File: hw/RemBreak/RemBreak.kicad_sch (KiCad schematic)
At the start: 5 parts, among them J1 Conn_02x06_Odd_Even, J2 Screw_Terminal_01x04, J3 Screw_Terminal_01x04

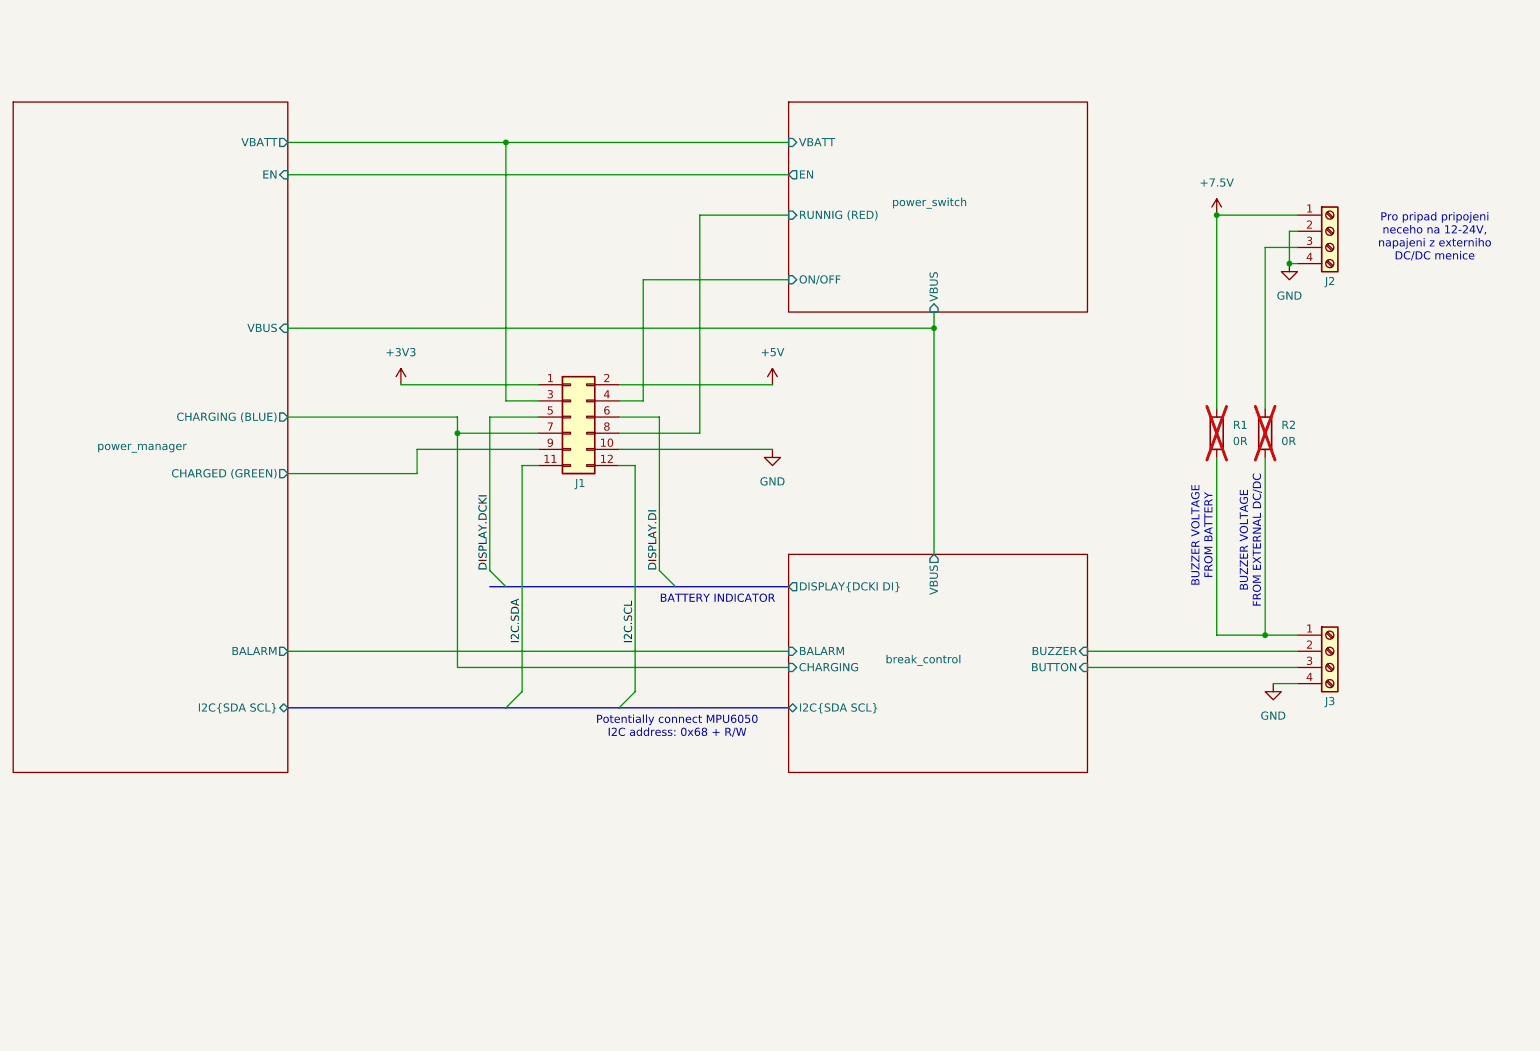
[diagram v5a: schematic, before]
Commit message: routing in progress added new subsheet to easily swap signals at the control connector
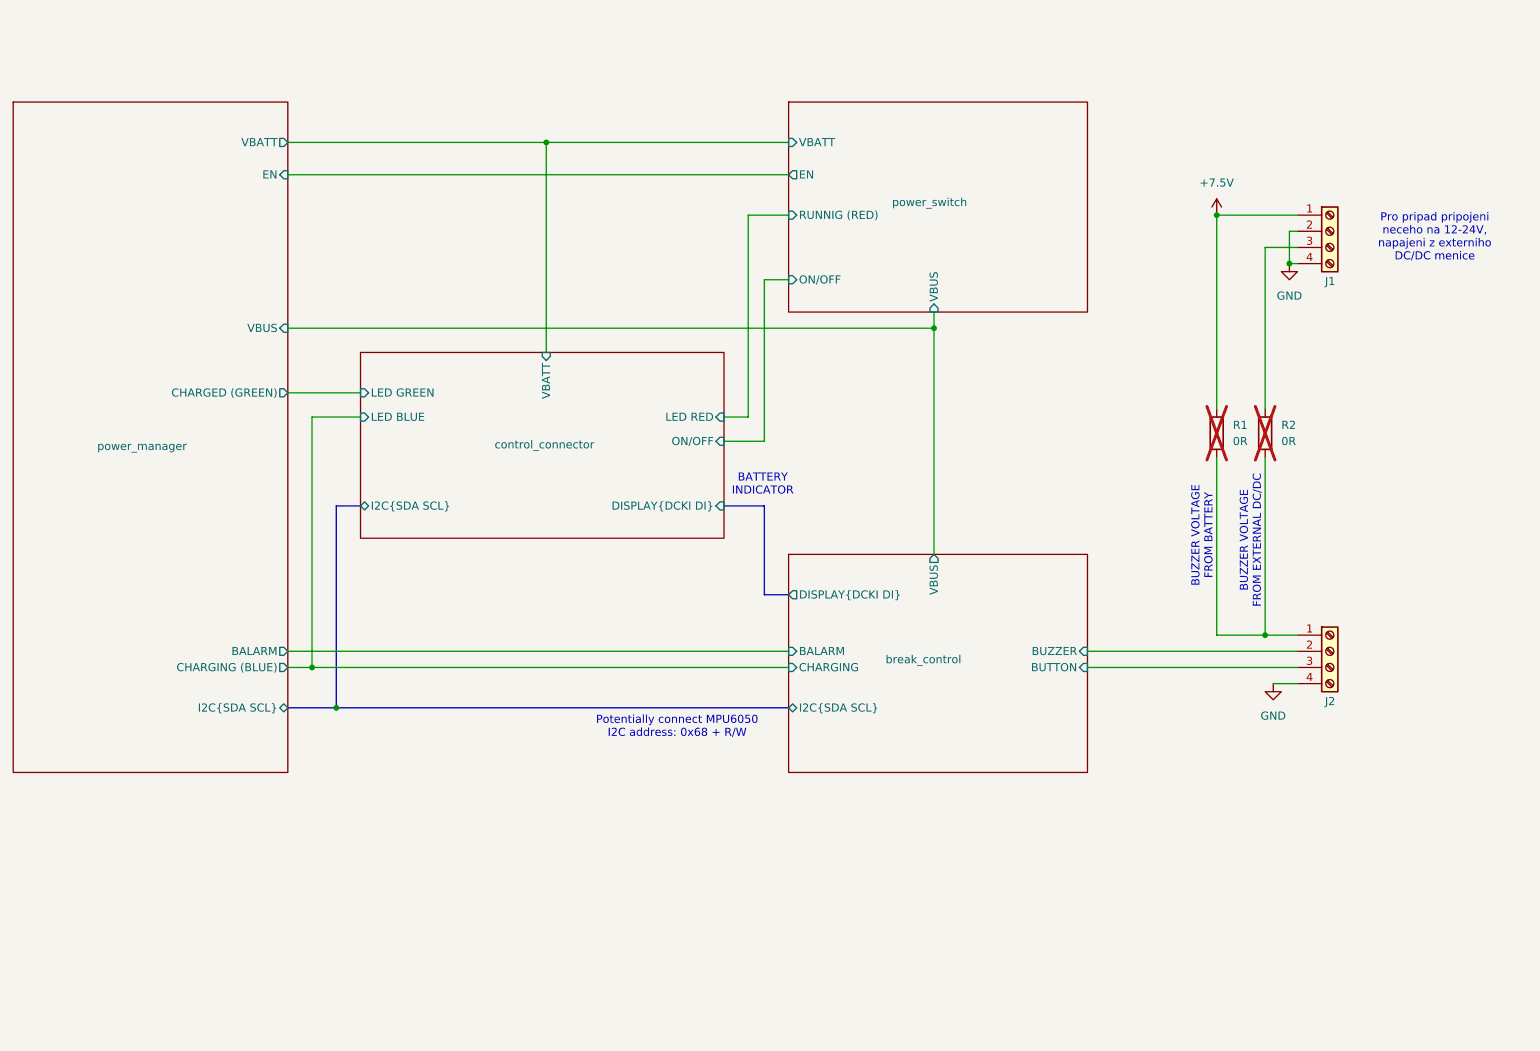
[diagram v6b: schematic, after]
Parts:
- removed J1: Conn_02x06_Odd_Even, chinese_modules:SAMTEC_TSM-106-01-L-DH-P-TR, symbol Connector_Generic:Conn_02x06_Odd_Even
- renumbered J2 to J1, J3 to J2
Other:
- added sheet control_connector (control_connector.kicad_sch)

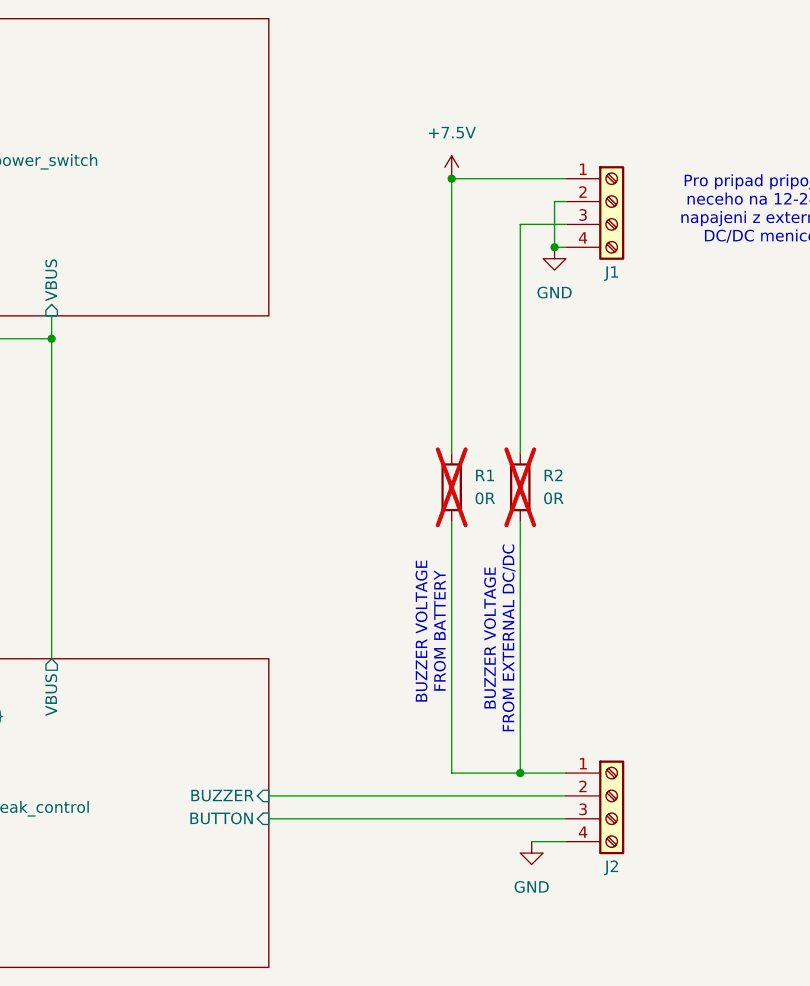
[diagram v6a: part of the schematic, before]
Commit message: first version of routing finished
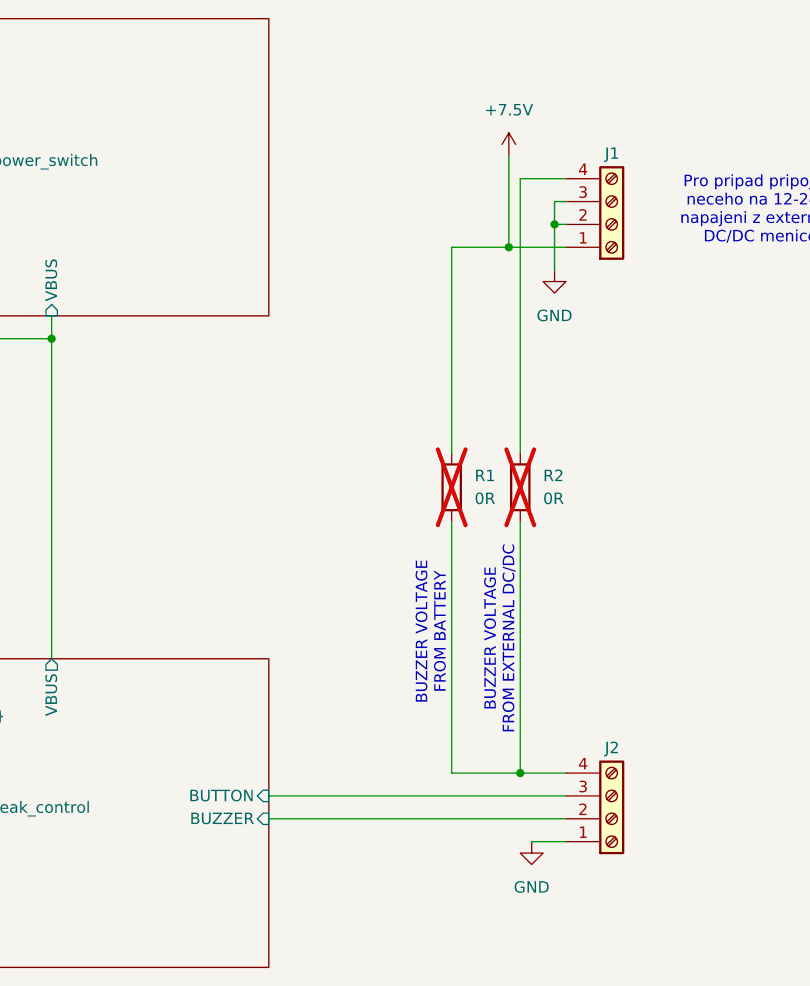
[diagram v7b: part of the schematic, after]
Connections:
- net GND: now also J1.3 (Pin_3), J2.1 (Pin_1); no longer J1.4 (Pin_4), J2.4 (Pin_4)
- net at R1.2, R2.2: now also J2.4 (Pin_4); no longer J2.1 (Pin_1)
- net at R2.1: now also J1.4 (Pin_4); no longer J1.3 (Pin_3)
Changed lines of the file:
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@@
+	)
+	(junction
+		(at 234.95 68.58)
+		(diameter 0)
+		(color 0 0 0 0)
 	)
 	(junction
@@
 	)
 	(junction
-		(at 184.15 78.74)
+		(at 240.03 66.04)
 		(diameter 0)
 		(color 0 0 0 0)
 	)
 	(junction
-		(at 240.03 68.58)
+		(at 184.15 78.74)
 		(diameter 0)
 		(color 0 0 0 0)
@@
 	)
 	(junction
-		(at 228.6 60.96)
-		(diameter 0)
-		(color 0 0 0 0)
-	)
-	(junction
 		(at 86.36 132.08)
 		(diameter 0)
@@
 	(wire
 		(pts
-			(xy 228.6 60.96) (xy 228.6 91.44)
-		)
-		(stroke
-			(width 0)
-			(type default)
-		)
-	)
-	(wire
-		(pts
 			(xy 82.55 129.54) (xy 161.29 129.54)
 		)
@@
 	(wire
 		(pts
+			(xy 234.95 68.58) (xy 241.3 68.58)
+		)
+		(stroke
+			(width 0)
+			(type default)
+		)
+	)
+	(wire
+		(pts
+			(xy 228.6 91.44) (xy 228.6 68.58)
+		)
+		(stroke
+			(width 0)
+			(type default)
+		)
+	)
+	(wire
+		(pts
 			(xy 228.6 127) (xy 236.22 127)
 		)
@@
 	(wire
 		(pts
+			(xy 236.22 60.96) (xy 241.3 60.96)
+		)
+		(stroke
+			(width 0)
+			(type default)
+		)
+	)
+	(wire
+		(pts
+			(xy 240.03 66.04) (xy 240.03 63.5)
+		)
+		(stroke
+			(width 0)
+			(type default)
+		)
+	)
+	(wire
+		(pts
 			(xy 236.22 127) (xy 241.3 127)
 		)
@@
 	(wire
 		(pts
+			(xy 236.22 91.44) (xy 236.22 60.96)
+		)
+		(stroke
+			(width 0)
+			(type default)
+		)
+	)
+	(wire
+		(pts
 			(xy 208.28 129.54) (xy 241.3 129.54)
 		)
@@
 	(wire
 		(pts
-			(xy 228.6 60.96) (xy 241.3 60.96)
-		)
-		(stroke
-			(width 0)
-			(type default)
-		)
-	)
-	(wire
-		(pts
 			(xy 82.55 132.08) (xy 86.36 132.08)
 		)
@@
 		)
 	)
+	(wire
+		(pts
+			(xy 234.95 58.42) (xy 234.95 68.58)
+		)
+		(stroke
+			(width 0)
+			(type default)
+		)
+	)
 	(bus
 		(pts
@@
 	(wire
 		(pts
-			(xy 240.03 68.58) (xy 241.3 68.58)
+			(xy 240.03 71.12) (xy 240.03 66.04)
+		)
+		(stroke
+			(width 0)
+			(type default)
+		)
+	)
+	(wire
+		(pts
+			(xy 228.6 68.58) (xy 234.95 68.58)
 		)
 		(stroke
@@
 	(wire
 		(pts
-			(xy 236.22 66.04) (xy 241.3 66.04)
+			(xy 240.03 66.04) (xy 241.3 66.04)
 		)
 		(stroke
@@
 		(pts
 			(xy 82.55 54.61) (xy 161.29 54.61)
-		)
-		(stroke
-			(width 0)
-			(type default)
-		)
-	)
-	(wire
-		(pts
-			(xy 240.03 63.5) (xy 240.03 68.58)
-		)
-		(stroke
-			(width 0)
-			(type default)
-		)
-	)
-	(wire
-		(pts
-			(xy 236.22 66.04) (xy 236.22 91.44)
 		)
 		(stroke
@@
 	(symbol
 		(lib_id "Connector:Screw_Terminal_01x04")
-		(at 246.38 129.54 0)
+		(at 246.38 132.08 0)
+		(mirror x)
 		(unit 1)
 		(exclude_from_sim no)
@@
 		(dnp no)
 		(property "Reference" "J2"
-			(at 245.618 137.414 0)
+			(at 245.618 124.206 0)
 			(effects
 				(font
@@
 		)
 		(property "Value" "Screw_Terminal_01x04"
-			(at 248.92 132.0799 0)
+			(at 248.92 129.5401 0)
 			(effects
 				(font
@@
 		)
 		(property "Footprint" "TerminalBlock_Phoenix:TerminalBlock_Phoenix_MPT-0,5-4-2.54_1x04_P2.54mm_Horizontal"
-			(at 246.38 129.54 0)
+			(at 246.38 132.08 0)
 			(effects
 				(font
@@
 		)
 		(property "Datasheet" "~"
-			(at 246.38 129.54 0)
+			(at 246.38 132.08 0)
 			(effects
 				(font
@@
 		)
 		(property "Description" "Generic screw terminal, single row, 01x04, script generated (kicad-library-utils/schlib/autogen/connector/)"
-			(at 246.38 129.54 0)
+			(at 246.38 132.08 0)
 			(effects
 				(font
@@
 	(symbol
 		(lib_id "power:GND")
-		(at 240.03 68.58 0)
+		(at 240.03 71.12 0)
 		(unit 1)
 		(exclude_from_sim no)
@@
 		(fields_autoplaced yes)
 		(property "Reference" "#PWR03"
-			(at 240.03 74.93 0)
+			(at 240.03 77.47 0)
 			(effects
 				(font
@@
 		)
 		(property "Value" "GND"
-			(at 240.03 73.66 0)
+			(at 240.03 76.2 0)
 			(effects
 				(font
@@
 		)
 		(property "Footprint" ""
-			(at 240.03 68.58 0)
+			(at 240.03 71.12 0)
 			(effects
 				(font
@@
 		)
 		(property "Datasheet" ""
-			(at 240.03 68.58 0)
+			(at 240.03 71.12 0)
 			(effects
 				(font
@@
 		)
 		(property "Description" "Power symbol creates a global label with name \"GND\" , ground"
-			(at 240.03 68.58 0)
+			(at 240.03 71.12 0)
 			(effects
 				(font
@@
 	(symbol
 		(lib_id "power:+7.5V")
-		(at 228.6 60.96 0)
+		(at 234.95 58.42 0)
 		(unit 1)
 		(exclude_from_sim no)
@@
 		(fields_autoplaced yes)
 		(property "Reference" "#PWR01"
-			(at 228.6 64.77 0)
+			(at 234.95 62.23 0)
 			(effects
 				(font
@@
 		)
 		(property "Value" "+7.5V"
-			(at 228.6 55.88 0)
+			(at 234.95 53.34 0)
 			(effects
 				(font
@@
 		)
 		(property "Footprint" ""
-			(at 228.6 60.96 0)
+			(at 234.95 58.42 0)
 			(effects
 				(font
@@
 		)
 		(property "Datasheet" ""
-			(at 228.6 60.96 0)
+			(at 234.95 58.42 0)
 			(effects
 				(font
@@
 		)
 		(property "Description" "Power symbol creates a global label with name \"+7.5V\""
-			(at 228.6 60.96 0)
+			(at 234.95 58.42 0)
 			(effects
 				(font
@@
 	(symbol
 		(lib_id "Connector:Screw_Terminal_01x04")
-		(at 246.38 63.5 0)
+		(at 246.38 66.04 0)
+		(mirror x)
 		(unit 1)
 		(exclude_from_sim no)
@@
 		(dnp no)
 		(property "Reference" "J1"
-			(at 245.618 71.374 0)
+			(at 245.618 58.166 0)
 			(effects
 				(font
@@
 		)
 		(property "Value" "Screw_Terminal_01x04"
-			(at 248.92 66.0399 0)
+			(at 248.92 63.5001 0)
 			(effects
 				(font
@@
 		)
 		(property "Footprint" "TerminalBlock_Phoenix:TerminalBlock_Phoenix_MPT-0,5-4-2.54_1x04_P2.54mm_Horizontal"
-			(at 246.38 63.5 0)
+			(at 246.38 66.04 0)
 			(effects
 				(font
@@
 		)
 		(property "Datasheet" "~"
-			(at 246.38 63.5 0)
+			(at 246.38 66.04 0)
 			(effects
 				(font
@@
 		)
 		(property "Description" "Generic screw terminal, single row, 01x04, script generated (kicad-library-utils/schlib/autogen/connector/)"
-			(at 246.38 63.5 0)
+			(at 246.38 66.04 0)
 			(effects
 				(font
@@
 		)
 		(pin "BUTTON" input
-			(at 208.28 132.08 0)
+			(at 208.28 129.54 0)
 			(effects
 				(font
@@
 		)
 		(pin "BUZZER" input
-			(at 208.28 129.54 0)
-			(effects
-				(font
+			(at 208.28 132.08 0)
+			(effects
+				(font

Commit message: changed board settings and replaced r and c footprints with the ones for handsoldering
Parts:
- R1, R2: footprint Resistor_SMD:R_0805_2012Metric -> Resistor_SMD:R_0805_2012Metric_Pad1.20x1.40mm_HandSolder
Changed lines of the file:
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@@
 			)
 		)
-		(property "Footprint" "Resistor_SMD:R_0805_2012Metric"
+		(property "Footprint" "Resistor_SMD:R_0805_2012Metric_Pad1.20x1.40mm_HandSolder"
 			(at 237.998 95.25 90)
 			(effects
@@
 			)
 		)
-		(property "Footprint" "Resistor_SMD:R_0805_2012Metric"
+		(property "Footprint" "Resistor_SMD:R_0805_2012Metric_Pad1.20x1.40mm_HandSolder"
 			(at 230.378 95.25 90)
 			(effects
